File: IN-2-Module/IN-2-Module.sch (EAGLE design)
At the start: 9 parts, among them T1 IN-2, T2 IN-2, U1 K155ID1, U2 K155ID1, U3 74HC595

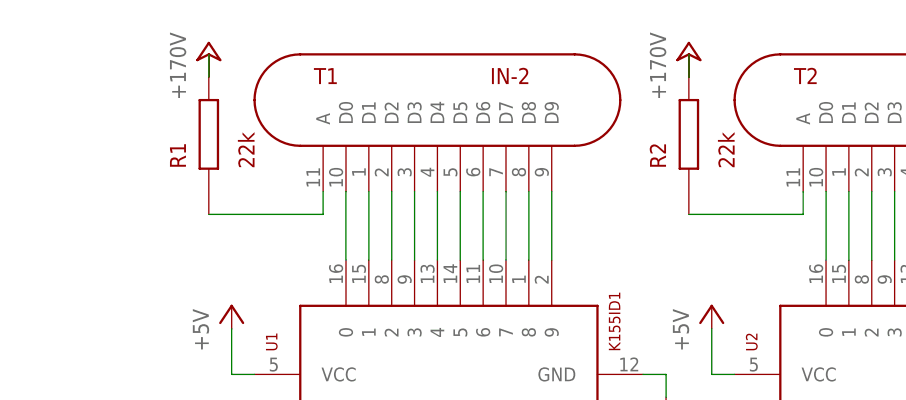
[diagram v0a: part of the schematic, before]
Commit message: Updated interconnect package.
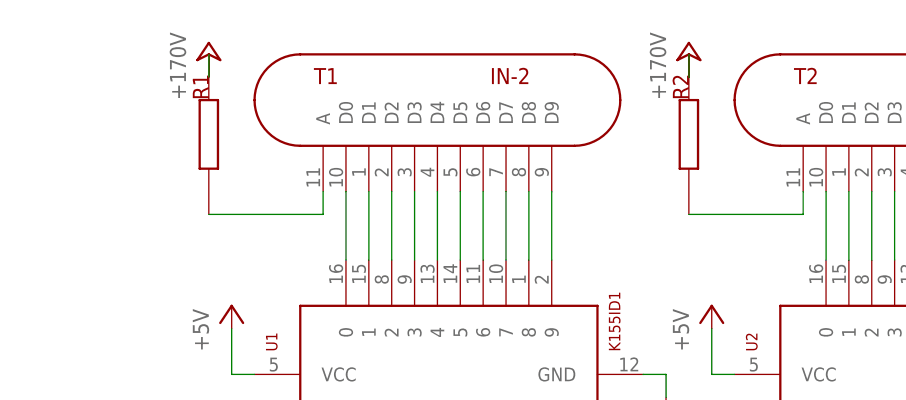
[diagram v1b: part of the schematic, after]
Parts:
- IN: value NIXIE_INTERCONNECT -> NIXIE_INTERCONNECTLEFT; device TimeExpander:NIXIE_INTERCONNECT -> TimeExpander:NIXIE_INTERCONNECTLEFT
- OUT: value NIXIE_INTERCONNECT -> NIXIE_INTERCONNECTRIGHT; device TimeExpander:NIXIE_INTERCONNECT -> TimeExpander:NIXIE_INTERCONNECTRIGHT
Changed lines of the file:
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@@
 <grid distance="0.1" unitdist="inch" unit="inch" style="lines" multiple="1" display="no" altdistance="0.01" altunitdist="inch" altunit="inch"/>
 <layers>
-<layer number="1" name="Top" color="4" fill="1" visible="no" active="no"/>
-<layer number="16" name="Bottom" color="1" fill="1" visible="no" active="no"/>
-<layer number="17" name="Pads" color="2" fill="1" visible="no" active="no"/>
-<layer number="18" name="Vias" color="2" fill="1" visible="no" active="no"/>
-<layer number="19" name="Unrouted" color="6" fill="1" visible="no" active="no"/>
-<layer number="20" name="Dimension" color="15" fill="1" visible="no" active="no"/>
-<layer number="21" name="tPlace" color="7" fill="1" visible="no" active="no"/>
-<layer number="22" name="bPlace" color="7" fill="1" visible="no" active="no"/>
-<layer number="23" name="tOrigins" color="15" fill="1" visible="no" active="no"/>
-<layer number="24" name="bOrigins" color="15" fill="1" visible="no" active="no"/>
-<layer number="25" name="tNames" color="7" fill="1" visible="no" active="no"/>
-<layer number="26" name="bNames" color="7" fill="1" visible="no" active="no"/>
-<layer number="27" name="tValues" color="7" fill="1" visible="no" active="no"/>
-<layer number="28" name="bValues" color="7" fill="1" visible="no" active="no"/>
+<layer number="1" name="Top" color="4" fill="1" visible="yes" active="no"/>
+<layer number="16" name="Bottom" color="1" fill="1" visible="yes" active="no"/>
+<layer number="17" name="Pads" color="2" fill="1" visible="yes" active="no"/>
+<layer number="18" name="Vias" color="2" fill="1" visible="yes" active="no"/>
+<layer number="19" name="Unrouted" color="6" fill="1" visible="yes" active="no"/>
+<layer number="20" name="Dimension" color="15" fill="1" visible="yes" active="no"/>
+<layer number="21" name="tPlace" color="7" fill="1" visible="yes" active="no"/>
+<layer number="22" name="bPlace" color="7" fill="1" visible="yes" active="no"/>
+<layer number="23" name="tOrigins" color="15" fill="1" visible="yes" active="no"/>
+<layer number="24" name="bOrigins" color="15" fill="1" visible="yes" active="no"/>
+<layer number="25" name="tNames" color="7" fill="1" visible="yes" active="no"/>
+<layer number="26" name="bNames" color="7" fill="1" visible="yes" active="no"/>
+<layer number="27" name="tValues" color="7" fill="1" visible="yes" active="no"/>
+<layer number="28" name="bValues" color="7" fill="1" visible="yes" active="no"/>
 <layer number="29" name="tStop" color="7" fill="3" visible="no" active="no"/>
 <layer number="30" name="bStop" color="7" fill="6" visible="no" active="no"/>
@@
 <layer number="35" name="tGlue" color="7" fill="4" visible="no" active="no"/>
 <layer number="36" name="bGlue" color="7" fill="5" visible="no" active="no"/>
-<layer number="37" name="tTest" color="7" fill="1" visible="no" active="no"/>
-<layer number="38" name="bTest" color="7" fill="1" visible="no" active="no"/>
+<layer number="37" name="tTest" color="7" fill="1" visible="yes" active="no"/>
+<layer number="38" name="bTest" color="7" fill="1" visible="yes" active="no"/>
 <layer number="39" name="tKeepout" color="4" fill="11" visible="no" active="no"/>
 <layer number="40" name="bKeepout" color="1" fill="11" visible="no" active="no"/>
@@
 <layer number="44" name="Drills" color="7" fill="1" visible="no" active="no"/>
 <layer number="45" name="Holes" color="7" fill="1" visible="no" active="no"/>
-<layer number="46" name="Milling" color="3" fill="1" visible="no" active="no"/>
-<layer number="47" name="Measures" color="7" fill="1" visible="no" active="no"/>
-<layer number="48" name="Document" color="7" fill="1" visible="no" active="no"/>
-<layer number="49" name="Reference" color="7" fill="1" visible="no" active="no"/>
-<layer number="50" name="dxf" color="7" fill="1" visible="no" active="no"/>
-<layer number="51" name="tDocu" color="7" fill="1" visible="no" active="no"/>
-<layer number="52" name="bDocu" color="7" fill="1" visible="no" active="no"/>
-<layer number="53" name="tGND_GNDA" color="7" fill="9" visible="no" active="no"/>
-<layer number="54" name="bGND_GNDA" color="1" fill="9" visible="no" active="no"/>
-<layer number="56" name="wert" color="7" fill="1" visible="no" active="no"/>
-<layer number="57" name="tCAD" color="7" fill="1" visible="no" active="no"/>
-<layer number="59" name="tCarbon" color="7" fill="1" visible="no" active="no"/>
-<layer number="60" name="bCarbon" color="7" fill="1" visible="no" active="no"/>
+<layer number="46" name="Milling" color="3" fill="1" visible="yes" active="no"/>
+<layer number="47" name="Measures" color="7" fill="1" visible="yes" active="no"/>
+<layer number="48" name="Document" color="7" fill="1" visible="yes" active="no"/>
+<layer number="49" name="Reference" color="7" fill="1" visible="yes" active="no"/>
+<layer number="50" name="dxf" color="7" fill="1" visible="yes" active="no"/>
+<layer number="51" name="tDocu" color="7" fill="1" visible="yes" active="no"/>
+<layer number="52" name="bDocu" color="7" fill="1" visible="yes" active="no"/>
+<layer number="53" name="tGND_GNDA" color="7" fill="9" visible="yes" active="no"/>
+<layer number="54" name="bGND_GNDA" color="1" fill="9" visible="yes" active="no"/>
+<layer number="56" name="wert" color="7" fill="1" visible="yes" active="no"/>
+<layer number="57" name="tCAD" color="7" fill="1" visible="yes" active="no"/>
+<layer number="59" name="tCarbon" color="7" fill="1" visible="yes" active="no"/>
+<layer number="60" name="bCarbon" color="7" fill="1" visible="yes" active="no"/>
 <layer number="90" name="Modules" color="5" fill="1" visible="yes" active="yes"/>
 <layer number="91" name="Nets" color="2" fill="1" visible="yes" active="yes"/>
@@
 <part name="T1" library="TimeExpander" deviceset="IN-2" device="" value="IN-2"/>
 <part name="T2" library="TimeExpander" deviceset="IN-2" device="" value="IN-2"/>
-<part name="OUT" library="TimeExpander" deviceset="NIXIE_INTERCONNECT" device=""/>
+<part name="OUT" library="TimeExpander" deviceset="NIXIE_INTERCONNECT" device="RIGHT" value="NIXIE_INTERCONNECTRIGHT"/>
 <part name="P+5" library="TimeExpander" deviceset="+170V" device=""/>
 <part name="GND3" library="TimeExpander" deviceset="GND" device=""/>
-<part name="IN" library="TimeExpander" deviceset="NIXIE_INTERCONNECT" device=""/>
+<part name="IN" library="TimeExpander" deviceset="NIXIE_INTERCONNECT" device="LEFT"/>
 </parts>
 <sheets>
